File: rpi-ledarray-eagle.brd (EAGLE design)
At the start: 33.5 x 19.2 mm, 27 parts

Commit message: First version finished
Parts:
- removed LED11, LED12, LED13: (no value), SparkFun:LED-1206
- removed R11, R12, R13, R14, R15, R16, R17: 270, SparkFun:1206
- added R1, R10, R2, R9: (no value), SparkFun:1206
- R3, R4, R5, R6, R7, R8: value 270 -> (none)
- moved LED2 24.1 mm to (7.67, 8.24)
- moved LED3 19.0 mm to (10.2, 8.24)
- moved R4 19.0 mm to (12.8, 2.65)
- moved LED7 16.6 mm to (20.4, 8.24)
- moved LED9 16.6 mm to (25.5, 8.24)
- moved R5 13.9 mm to (15.3, 2.65)
- moved R3 8.99 mm to (10.2, 2.65)
- moved R7 8.99 mm to (20.4, 2.65)
- moved LED10 6.46 mm to (28.0, 8.24)
- moved R8 6.46 mm to (22.9, 2.65)
- moved LED5 3.96 mm to (15.3, 8.24)
- moved LED1 3.96 mm to (5.13, 8.24)
- moved R6 3.96 mm to (17.8, 2.65)
- moved LED8 3.96 mm to (22.9, 8.24)
- moved JP1 2.85 mm to (16.6, 14.4)
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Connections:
- removed net N$16: LED12.A, R16.2
- removed net N$17: LED13.A, R17.2
- removed net N$7: LED5.A, R7.2
- removed net N$8: LED6.A, R8.2
- new net 3V3_1: JP1.1
- new net 3V3_2: JP1.17
- new net N$10: LED10.A, R10.2
- net 5V: now also R1.1, R10.1, R2.1, R9.1; no longer R11.1, R12.1, R13.1, R14.1, R15.1, R16.1, R17.1
- net GPIO10_MOSI: no longer LED5.C
- net GPIO11_SCLK: no longer LED6.C
- net GPIO17: now also LED2.C; no longer LED7.C
- net GPIO18: now also LED5.C; no longer LED8.C
- net GPIO22: now also LED4.C; no longer LED9.C
- net GPIO23: now also LED6.C; no longer LED10.C
- net GPIO24: now also LED7.C; no longer LED11.C
- net GPIO25: now also LED8.C; no longer LED12.C
- net GPIO27: now also LED3.C; no longer LED13.C
- net GPIO7: now also LED10.C; no longer LED2.C
- net GPIO8: now also LED9.C; no longer LED3.C
- net GPIO9_MISO: no longer LED4.C
- net N$11: now also LED9.A, R9.2; no longer LED7.A, R11.2
- net N$12: now also R8.2; no longer R12.2
- net N$13: now also LED7.A, R7.2; no longer LED9.A, R13.2
- net N$14: now also LED6.A, R6.2; no longer LED10.A, R14.2
- net N$15: now also LED5.A, R5.2; no longer LED11.A, R15.2
- net N$3: now also R1.2; no longer R3.2
- net N$4: now also R3.2; no longer R5.2
- net N$5: now also R2.2; no longer R4.2
- net N$6: now also R4.2; no longer R6.2
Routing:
- net GPIO11_SCLK: track 16.4 -> 0.00 mm
- net GPIO10_MOSI: track 15.5 -> 0.00 mm
- net GPIO9_MISO: track 14.9 -> 0.00 mm
- net 5V: track 50.5 -> 42.0 mm, vias 1 -> 0
- net GPIO17: track 13.0 -> 7.77 mm
- net GPIO4: track 10.4 -> 5.22 mm
- net GND: track 17.3 -> 12.3 mm
- net GPIO18: track 11.2 -> 6.50 mm
- net GPIO27: track 12.4 -> 7.76 mm
- net N$8: track 2.69 -> 0.00 mm
- net N$7: track 2.69 -> 0.00 mm
- net N$17: track 2.69 -> 0.00 mm
- net N$16: track 2.69 -> 0.00 mm
- net N$10: track 0.00 -> 2.69 mm
- net GPIO22: track 12.4 -> 9.90 mm
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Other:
- board size 33.5 x 19.2 mm -> 33.1 x 17 mm
- board text added: "R. Nugent prizepony.us"
- board text added: "RPi LED Array"

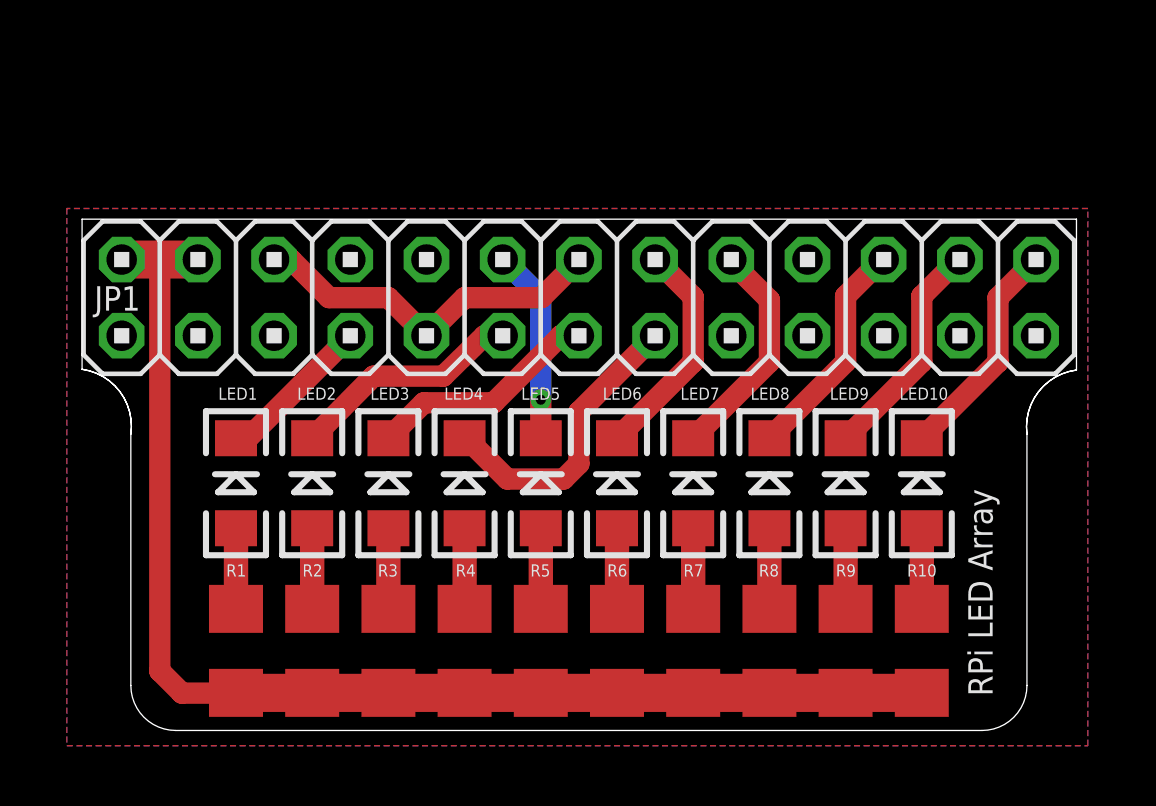
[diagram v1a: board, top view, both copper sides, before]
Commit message: Adjusted board dimensions. Adjusted font size and placement.
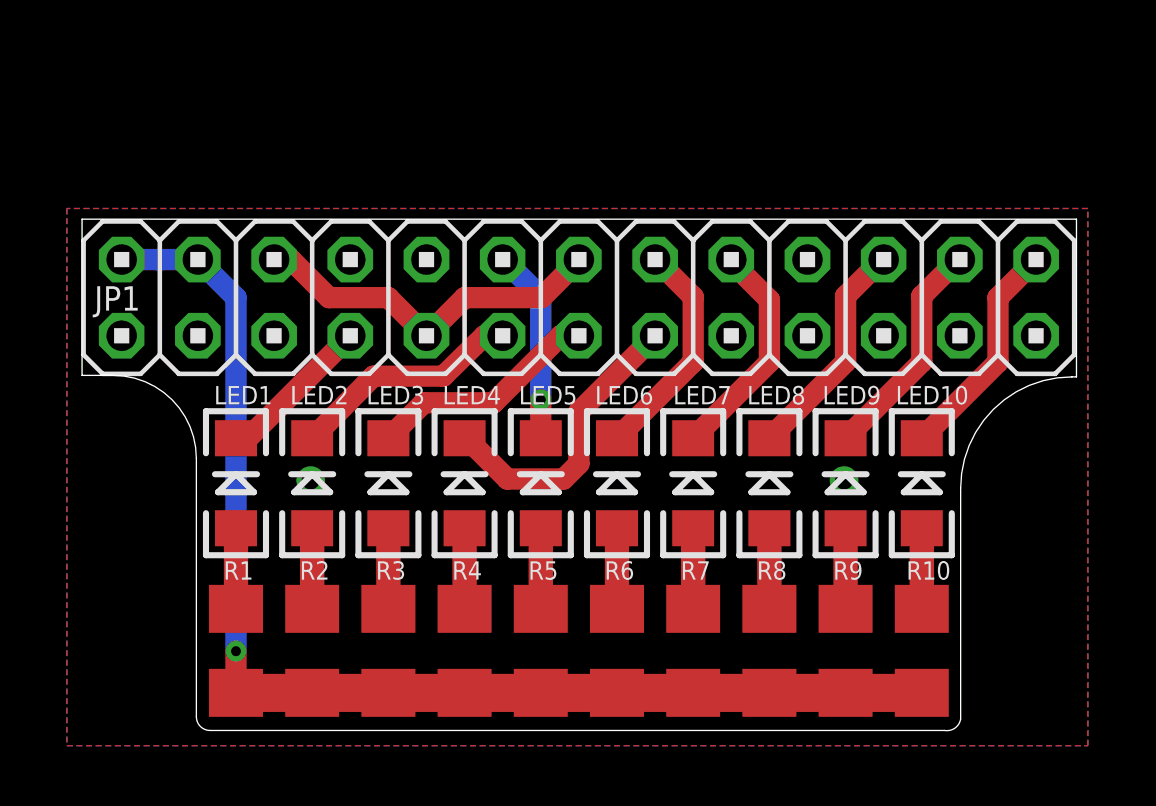
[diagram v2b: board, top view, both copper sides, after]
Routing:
- net 5V: track 42.0 -> 40.4 mm, vias 0 -> 1
- net GND: vias 0 -> 2
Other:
- outline, holes or cut-outs redrawn
- board text added: "R. Nugent prizepony.us 2013"
- board text removed: "R. Nugent prizepony.us"

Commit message: Changed resistors to 0603. Shrunk the board dimensions.
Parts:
- R1, R10, R2, R3, R4, R5, R6, R7, R8, R9: device SparkFun:1206 -> SparkFun:0603-RES
- moved R1 0.51 mm to (5.13, 3.16)
- moved R10 0.51 mm to (28.0, 3.16)
- moved R2 0.51 mm to (7.67, 3.16)
- moved R3 0.51 mm to (10.2, 3.16)
- moved R4 0.51 mm to (12.8, 3.16)
- moved R5 0.51 mm to (15.3, 3.16)
- moved R6 0.51 mm to (17.8, 3.16)
- moved R7 0.51 mm to (20.4, 3.16)
- moved R8 0.51 mm to (22.9, 3.16)
- moved R9 0.51 mm to (25.5, 3.16)
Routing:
- net 5V: track 40.4 -> 39.9 mm
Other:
- board size 33.1 x 17 mm -> 33.1 x 15.8 mm
